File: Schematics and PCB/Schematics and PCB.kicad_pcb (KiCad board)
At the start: 4 copper layers, 181 x 150 mm, 599 parts, among them J11 Conn_01x12, J6 UPSTREAM, J7 DOWNSTREAM_3, J8 DOWNSTREAM_1, J9 DOWNSTREAM_2, Q1 FDN340P, Q2 FDN340P, Q3 FDN340P, Q4 FS8205, SW10 1, SW100 NUMPAD15, SW101 NUMPAD16, SW102 NUMPAD17, SW103 NUMPAD18, SW104 NUMPAD19, SW105 NUMPAD20, SW108 Battery Switch, SW11 2, SW12 3, SW13 4, SW14 5, SW15 6, SW16 TAB, SW17 Q, SW18 W, SW19 E, SW2 ESC, SW20 R, SW21 T, SW22 MAYUS, SW23 A, SW24 S, SW25 D, SW26 F, SW27 G, SW28 L_SHIFT, SW29 Z, SW3 F1, SW30 X, SW31 C, SW32 V, SW33 B, SW34 L_CRTL, SW35 OS, SW36 L_ALT, SW37 L_SPACE, SW38 F7, SW39 F8, SW4 F2, SW40 F9, SW41 F10, SW42 F11, SW43 F12, SW44 PRT_SCR, SW45 DEL, SW46 7, SW47 8, SW48 9, SW49 0, SW5 F3, SW50 -, SW51 =, SW52 BACKSPACE, SW53 MACRO1, SW54 Y, SW55 U, SW56 I, SW57 O, SW58 P, SW59 [, SW6 F4, SW60 ], SW61 \, SW62 H, SW63 J, SW64 K, SW65 L, SW66 ;, SW67 ', SW68 ENTER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

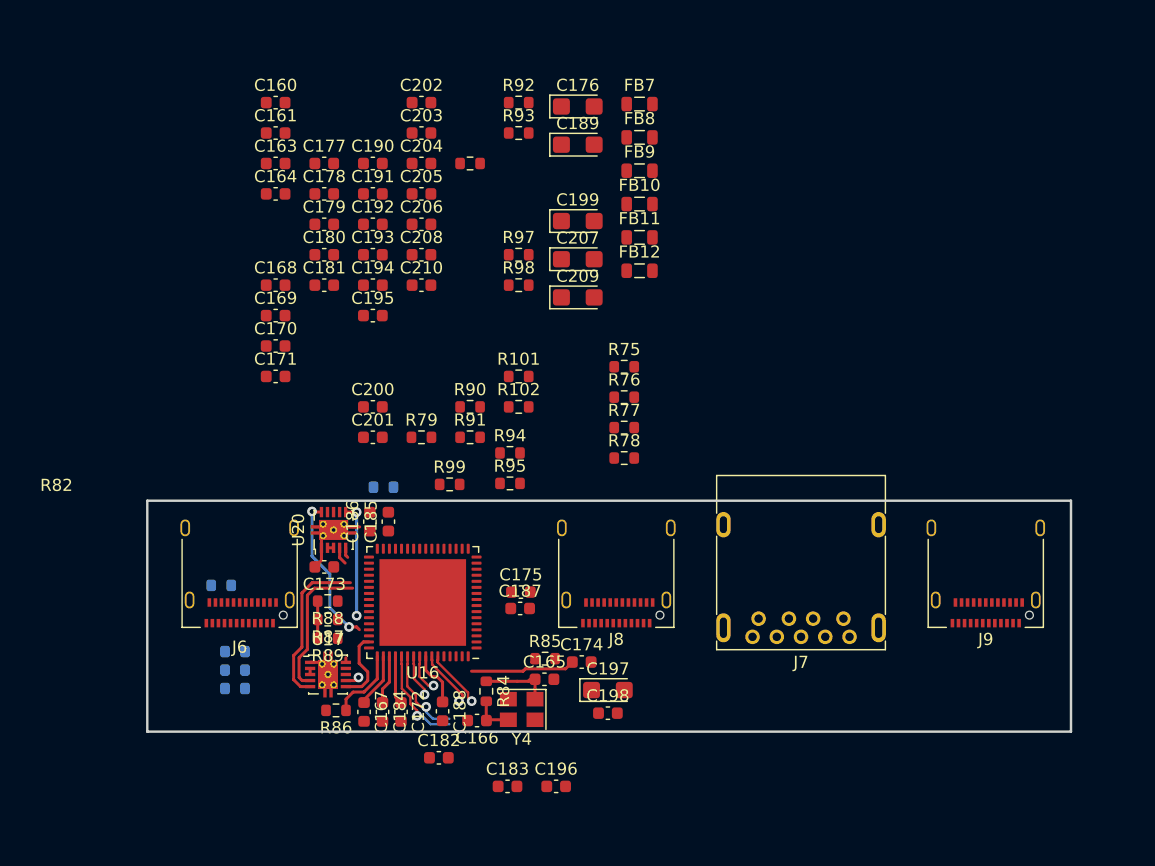
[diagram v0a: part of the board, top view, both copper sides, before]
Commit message: route most of the differential pairs
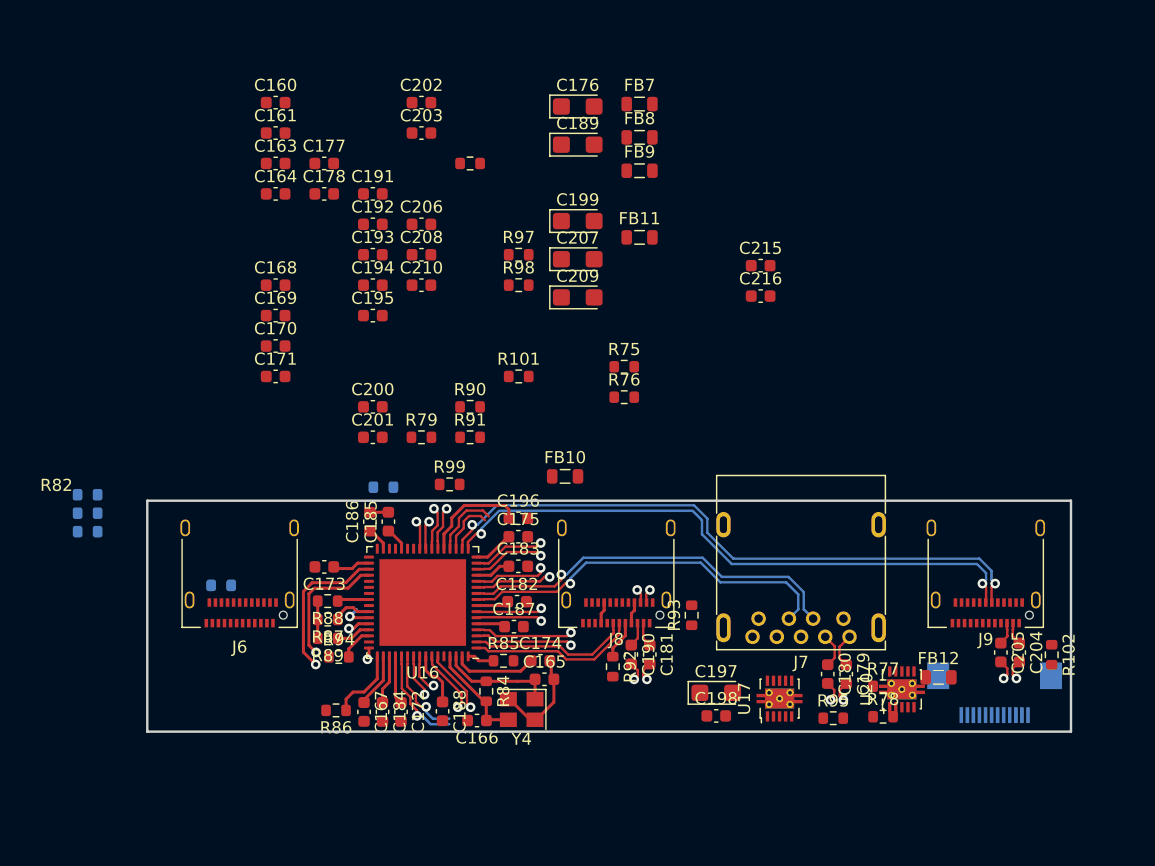
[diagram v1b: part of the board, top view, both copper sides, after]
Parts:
- added C215: 100n, Capacitor_SMD:C_0603_1608Metric, F.Cu at (260.1, 75.9)
- added C216: 100n, Capacitor_SMD:C_0603_1608Metric, F.Cu at (260.1, 78.4)
- added J10: Conn_01x12, Connector_FFC-FPC:Hirose_FH12-12S-0.5SH_1x12-1MP_P0.50mm_Horizontal, B.Cu at (279.4, 111.1)
- moved C204 63.7 mm to (281.5, 107.8), turned to -90 degrees
- moved C205 61.0 mm to (280.0, 107.8), turned to -90 degrees
- moved C179 56.8 mm to (267.2, 109.6), turned to -90 degrees
- moved C180 54.1 mm to (265.7, 109.6), turned to -90 degrees
- moved U20 48.7 mm to (271.8, 110.8)
- moved R102 48.5 mm to (284.2, 108.0), turned to -90 degrees
- moved R92 47.2 mm to (248.0, 108.9), turned to -90 degrees
- moved C190 45.8 mm to (249.5, 107.9), turned to -90 degrees
- moved R93 42.3 mm to (254.5, 104.7), turned to 90 degrees
- moved FB12 41.6 mm to (274.8, 109.8)
- moved C181 40.6 mm to (251.0, 107.9), turned to -90 degrees
- moved U17 37.3 mm to (261.7, 111.6), turned to 90 degrees
- moved R95 33.0 mm to (266.1, 113.2)
- moved R77 30.2 mm to (270.2, 110.6)
- moved R78 30.2 mm to (270.2, 113.1)
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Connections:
- C179 pad 1: /USB Hub/DN3_SSTX_CAP_P -> /USB Hub/DN2_SSTX_CAP_P
- C179 pad 2: /USB Hub/DN3_SSTX_P -> /USB Hub/DN2_SSTX_P
- C180 pad 1: /USB Hub/DN3_SSTX_CAP_N -> /USB Hub/DN2_SSTX_CAP_N
- C180 pad 2: /USB Hub/DN3_SSTX_N -> /USB Hub/DN2_SSTX_N
- C201 pad 1: /USB Hub/DN2_VBUS -> /USB Hub/DN3_VBUS
- C204 pad 1: /USB Hub/DN2_SSTX_CAP_P -> /USB Hub/DN3_SSTX_CAP_P
- C204 pad 2: /USB Hub/DN2_SSTX_P -> /USB Hub/DN3_SSTX_P
- C205 pad 1: /USB Hub/DN2_SSTX_CAP_N -> /USB Hub/DN3_SSTX_CAP_N
- C205 pad 2: /USB Hub/DN2_SSTX_N -> /USB Hub/DN3_SSTX_N
- FB12 pad 2: /USB Hub/DN2_VBUS -> /USB Hub/DN3_VBUS
- J7 pad 2: /USB Hub/DN3_N -> /USB Hub/DN2_N
- J7 pad 3: /USB Hub/DN3_P -> /USB Hub/DN2_P
- J7 pad 5: /USB Hub/DN3_SSRX_N -> /USB Hub/DN2_SSRX_N
- J7 pad 6: /USB Hub/DN3_SSRX_P -> /USB Hub/DN2_SSRX_P
- J7 pad 8: /USB Hub/DN3_SSTX_CAP_N -> /USB Hub/DN2_SSTX_CAP_N
- J7 pad 9: /USB Hub/DN3_SSTX_CAP_P -> /USB Hub/DN2_SSTX_CAP_P
- J9 pad A2: /USB Hub/DN2_SSTX_CAP_P -> /USB Hub/DN3_SSTX_CAP_P
- J9 pad A3: /USB Hub/DN2_SSTX_CAP_N -> /USB Hub/DN3_SSTX_CAP_N
- J9 pad A6: /USB Hub/DN2_P -> /USB Hub/DN3_P
- J9 pad A7: /USB Hub/DN2_N -> /USB Hub/DN3_N
- J9 pad B10: /USB Hub/DN2_SSRX_N -> /USB Hub/DN3_SSRX_N
- J9 pad B11: /USB Hub/DN2_SSRX_P -> /USB Hub/DN3_SSRX_P
- J9 pad B6: /USB Hub/DN2_P -> /USB Hub/DN3_P
- J9 pad B7: /USB Hub/DN2_N -> /USB Hub/DN3_N
- U16 pad 24: /Main IC1/D+ -> /USB Hub/DN4_P
- U16 pad 25: /Main IC1/D- -> /USB Hub/DN4_N
- U16 pad 26: unconnected-(U16-USB_SSTXP_DN4-Pad26) -> /USB Hub/DN4_SSTX_P
- U16 pad 27: unconnected-(U16-USB_SSTXM_DN4-Pad27) -> /USB Hub/DN4_SSTX_N
- U16 pad 29: unconnected-(U16-USB_SSRXP_DN4-Pad29) -> /USB Hub/DN4_SSRX_P
- U16 pad 30: unconnected-(U16-USB_SSRXM_DN4-Pad30) -> /USB Hub/DN4_SSRX_N
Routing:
- net /USB Hub/DN3_SSTX_N: track 0.00 -> 55.6 mm, vias 0 -> 1
- net /USB Hub/DN3_SSTX_P: track 0.00 -> 55.3 mm, vias 0 -> 1
- net /USB Hub/DN3_N: track 0.00 -> 51.6 mm, vias 0 -> 2
- net /USB Hub/DN3_P: track 0.00 -> 50.1 mm, vias 0 -> 2
- net /USB Hub/DN2_SSTX_P: track 0.00 -> 43.4 mm, vias 0 -> 2
- net /USB Hub/DN2_SSTX_N: track 0.00 -> 42.6 mm, vias 0 -> 2
- net /USB Hub/DN2_SSRX_P: track 0.00 -> 33.7 mm, vias 0 -> 1
- net /USB Hub/DN1_SSRX_P: track 0.00 -> 33.5 mm, vias 0 -> 2
- net /USB Hub/DN2_SSRX_N: track 0.00 -> 32.9 mm, vias 0 -> 1
- net /USB Hub/DN1_SSRX_N: track 0.00 -> 32.7 mm, vias 0 -> 2
- net /USB Hub/DN2_N: track 0.00 -> 32.2 mm, vias 0 -> 1
- net /USB Hub/DN2_P: track 0.00 -> 31.5 mm, vias 0 -> 1
- net /USB Hub/1V1_HUB: track 8.63 -> 29.5 mm
- net /USB Hub/DN1_SSTX_P: track 0.00 -> 20.4 mm, vias 0 -> 2
- net /USB Hub/DN1_SSTX_N: track 0.00 -> 19.7 mm, vias 0 -> 2
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
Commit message: Differential pairs routed on the hub
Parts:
- R82: moved to B.Cu
- moved C189 66.9 mm to (200.2, 115.6)
- moved R96 59.3 mm to (261.4, 114.8)
- moved C176 58.7 mm to (214.1, 112.5), turned to 180 degrees
- moved FB10 44.2 mm to (205.7, 115.3)
- moved C163 42.5 mm to (222.3, 109.9), turned to -90 degrees
- moved C164 40.0 mm to (220.8, 109.9), turned to -90 degrees
- moved C215 38.9 mm to (277.1, 110.9), turned to -90 degrees
- moved R82 38.3 mm to (215.7, 99.7), turned to 180 degrees
- moved C216 37.5 mm to (278.9, 110.9), turned to -90 degrees
- moved FB7 18.5 mm to (232.2, 66.6)
- moved R102 13.8 mm to (273.0, 116.1)
- moved R100 11.1 mm to (218.3, 91.2)
- moved C185 5.33 mm to (224.2, 97.6), turned to 180 degrees
- moved C186 4.35 mm to (224.2, 99.2), turned to 180 degrees
- moved FB12 3.03 mm to (272.7, 107.7)
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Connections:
- C172 pad 1: +3V3 -> /USB Hub/3V3_HUB_FILTER
- C173 pad 1: +3V3 -> /USB Hub/3V3_HUB_FILTER
- C174 pad 1: +3V3 -> /USB Hub/3V3_HUB_FILTER
- C175 pad 1: +3V3 -> /USB Hub/3V3_HUB_FILTER
- C176 pad 1: +3V3 -> /USB Hub/3V3_HUB_FILTER
- C182 pad 1: /USB Hub/1V1_HUB -> /USB Hub/1V1_HUB_FILTER
- C183 pad 1: /USB Hub/1V1_HUB -> /USB Hub/1V1_HUB_FILTER
- C184 pad 1: /USB Hub/1V1_HUB -> /USB Hub/1V1_HUB_FILTER
- C185 pad 1: /USB Hub/1V1_HUB -> /USB Hub/1V1_HUB_FILTER
- C186 pad 1: /USB Hub/1V1_HUB -> /USB Hub/1V1_HUB_FILTER
- C187 pad 1: /USB Hub/1V1_HUB -> /USB Hub/1V1_HUB_FILTER
- C188 pad 1: /USB Hub/1V1_HUB -> /USB Hub/1V1_HUB_FILTER
- C189 pad 1: /USB Hub/1V1_HUB -> /USB Hub/1V1_HUB_FILTER
- C203 pad 1: +3V3 -> /USB Hub/3V3_HUB
- FB10 pad 2: /USB Hub/1V1_HUB -> /USB Hub/1V1_HUB_FILTER
- FB7 pad 1: +3V3 -> /USB Hub/3V3_HUB
- FB7 pad 2: +3V3 -> /USB Hub/3V3_HUB_FILTER
- U16 pad 13: /USB Hub/1V1_HUB -> /USB Hub/1V1_HUB_FILTER
- U16 pad 16: +3V3 -> /USB Hub/3V3_HUB_FILTER
- U16 pad 21: /USB Hub/1V1_HUB -> /USB Hub/1V1_HUB_FILTER
- U16 pad 28: /USB Hub/1V1_HUB -> /USB Hub/1V1_HUB_FILTER
- U16 pad 31: /USB Hub/1V1_HUB -> /USB Hub/1V1_HUB_FILTER
- U16 pad 34: +3V3 -> /USB Hub/3V3_HUB_FILTER
- U16 pad 5: /USB Hub/1V1_HUB -> /USB Hub/1V1_HUB_FILTER
- U16 pad 51: /USB Hub/1V1_HUB -> /USB Hub/1V1_HUB_FILTER
- U16 pad 52: +3V3 -> /USB Hub/3V3_HUB_FILTER
- U16 pad 57: /USB Hub/1V1_HUB -> /USB Hub/1V1_HUB_FILTER
- U16 pad 63: +3V3 -> /USB Hub/3V3_HUB_FILTER
- U16 pad 8: /USB Hub/1V1_HUB -> /USB Hub/1V1_HUB_FILTER
- U19 pad 5: +3V3 -> /USB Hub/3V3_HUB
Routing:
- net /USB Hub/DN4_P: track 2.37 -> 81.3 mm
- net /USB Hub/DN4_N: track 2.37 -> 79.9 mm
- net /USB Hub/DN4_SSRX_P: track 0.00 -> 75.6 mm, vias 0 -> 2
- net /USB Hub/DN4_SSRX_N: track 0.00 -> 74.8 mm, vias 0 -> 2
- net /USB Hub/DN4_SSTX_N: track 0.00 -> 72.3 mm, vias 0 -> 2
- net /USB Hub/DN4_SSTX_P: track 0.00 -> 70.8 mm, vias 0 -> 2
- net /USB Hub/UP_P: track 8.38 -> 65.0 mm, vias 1 -> 3
- net /USB Hub/DN3_SSRX_N: track 3.62 -> 59.7 mm, vias 1 -> 2
- net /USB Hub/DN3_SSRX_P: track 3.62 -> 59.6 mm, vias 1 -> 2
- net /USB Hub/UP_N: track 7.64 -> 60.3 mm, vias 1 -> 3
- net /USB Hub/UP_SSRX_N: track 5.34 -> 41.6 mm, vias 1 -> 2
- net /USB Hub/UP_SSRX_P: track 5.34 -> 40.2 mm, vias 1 -> 2
- net /USB Hub/1V1_HUB_FILTER: track 0.00 -> 30.3 mm
- net GND: track 1422.4 -> 1450.3 mm, vias 26 -> 30
- net /USB Hub/UP_VBUS: track 0.00 -> 25.3 mm
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
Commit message: restarted hub layout
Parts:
- added C162: 10u, Capacitor_Tantalum_SMD:CP_EIA-3216-18_Kemet-A, F.Cu at (408.0, 144.2)
- C160, C161, C168, C169, C170, C171, C176, C189, C191, C192, C193, C194, C197, C198, C199, C200, C206, C207, C208, C209, C210, C215, C216, FB10, FB11, FB7, R101, R102, R79, R90, R91, R92, R93, R94, R95, R97, R98, R99, U17, U20: moved to B.Cu
- R80, R81: moved to F.Cu
- moved U18 334.8 mm to (493.4, 140.3)
- moved U19 330.0 mm to (493.4, 133.7), turned to 180 degrees
- moved C191 274.9 mm to (492.6, 145.1), turned to 180 degrees
- moved C195 273.6 mm to (496.3, 134.5), turned to -90 degrees
- moved C203 270.8 mm to (493.4, 136.2)
- moved C202 269.7 mm to (490.6, 139.6), turned to 90 degrees
- moved R100 263.7 mm to (478.4, 134.6), turned to -90 degrees
- moved C194 263.7 mm to (485.9, 133.5), turned to 90 degrees
- moved C192 261.9 mm to (482.8, 133.5), turned to 90 degrees
- moved C177 260.5 mm to (471.6, 148.8), turned to 90 degrees
- moved C201 258.3 mm to (480.4, 145.6)
- moved FB11 256.0 mm to (495.9, 145.1), turned to 180 degrees
- moved C196 255.6 mm to (493.4, 137.8), turned to 180 degrees
- moved C210 254.8 mm to (477.9, 144.9)
- moved R98 253.2 mm to (486.6, 135.8)
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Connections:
- FB11 pad 1: /V_USB -> /USB Hub/DN4_CONN
- J10 pad 1: /USB Hub/DN4_VBUS -> /USB Hub/DN4_CONN
- J10 pad 2: /USB Hub/DN4_VBUS -> /USB Hub/DN4_CONN
- J10 pad 5: unconnected-(J10-Pin_5-Pad5) -> /USB Hub/1V1_EN
- J10 pad 6: /USB Hub/DN4_P -> /USB Hub/3V3_EN
- J10 pad 7: /USB Hub/DN4_N -> /USB Hub/DN4_P
- J10 pad 8: unconnected-(J10-Pin_8-Pad8) -> /USB Hub/DN4_N
- J6 pad S1: (no net) -> Net-(J6-Shield)
- J8 pad S1: (no net) -> Net-(J8-Shield)
- J9 pad S1: (no net) -> Net-(J9-Shield)
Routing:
- net GND: track 1450.3 -> 1640.7 mm, vias 30 -> 36
- net /USB Hub/UP_VBUS: track 25.3 -> 187.2 mm, vias 0 -> 6
- net /USB Hub/DN4_P: track 81.3 -> 7.35 mm
- net /USB Hub/DN4_N: track 79.9 -> 6.23 mm
- net /USB Hub/DN4_SSTX_N: track 72.3 -> 2.20 mm, vias 2 -> 1
- net /USB Hub/DN4_SSRX_N: track 74.8 -> 5.59 mm, vias 2 -> 1
- net /USB Hub/DN4_SSRX_P: track 75.6 -> 6.42 mm, vias 2 -> 1
- net /USB Hub/DN4_SSTX_P: track 70.8 -> 2.20 mm, vias 2 -> 1
- net /USB Hub/DN3_SSTX_P: track 69.6 -> 1.67 mm, vias 2 -> 1
- net /USB Hub/DN3_SSTX_N: track 68.9 -> 1.67 mm, vias 2 -> 1
- net /USB Hub/3V3_HUB: track 0.00 -> 58.6 mm, vias 0 -> 1
- net /USB Hub/DN3_SSRX_N: track 59.7 -> 2.32 mm, vias 2 -> 1
- net /USB Hub/DN3_SSRX_P: track 59.6 -> 2.32 mm, vias 2 -> 1
- net /USB Hub/~{OVCURR2}: track 2.78 -> 58.4 mm, vias 1 -> 3
- net /USB Hub/~{OVCURR1}: track 2.79 -> 54.8 mm, vias 0 -> 3
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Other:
- board size 181 x 150 mm -> 339.6 x 114.3 mm

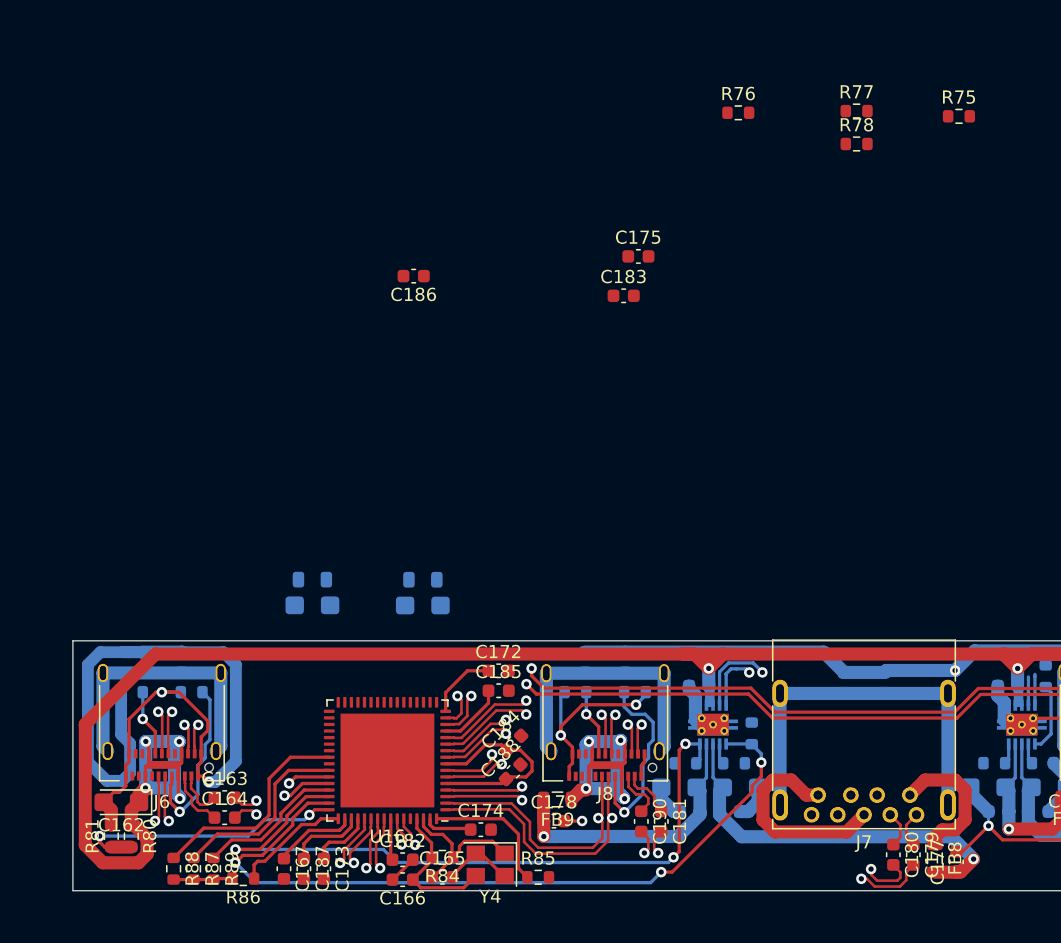
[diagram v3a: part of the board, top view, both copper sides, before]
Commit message: More Hub routing
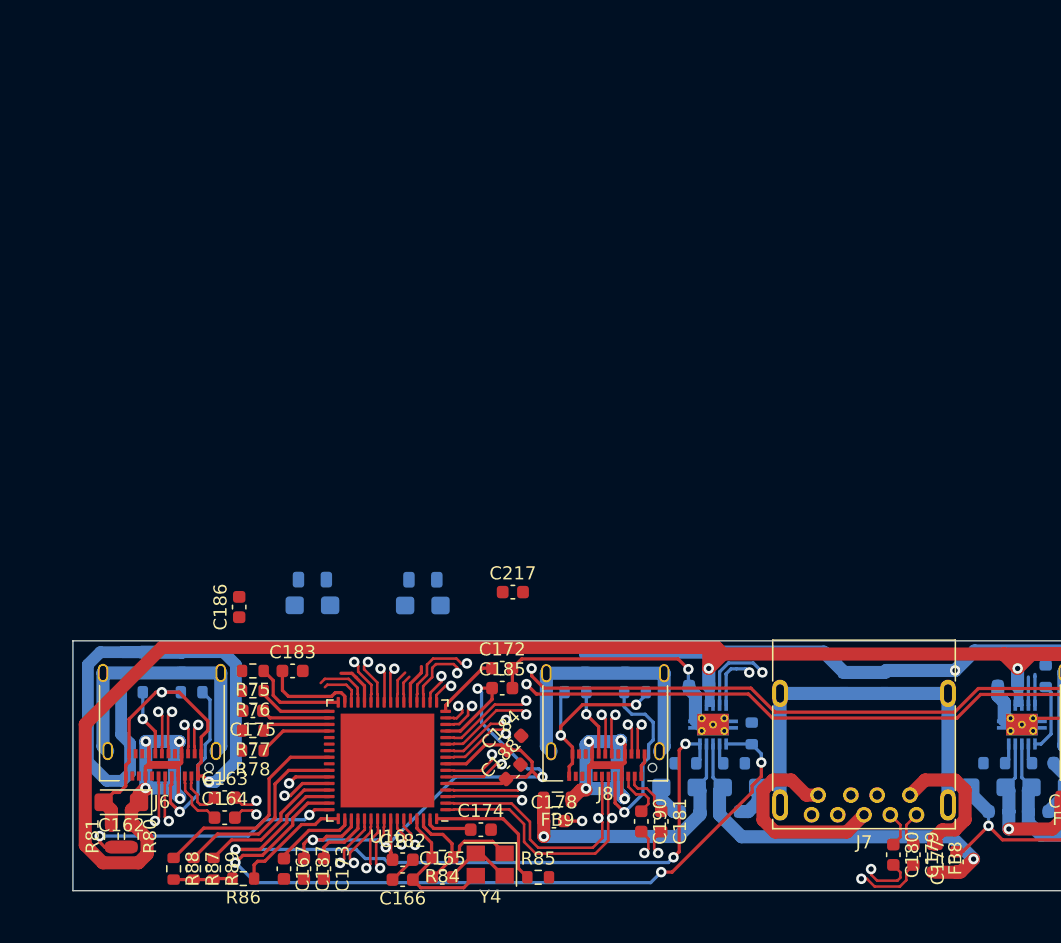
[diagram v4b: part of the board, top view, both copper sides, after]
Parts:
- added C217: 100n, Capacitor_SMD:C_0603_1608Metric, F.Cu at (437.8, 128.2)
- moved R75 68.4 mm to (418.0, 134.2), turned to 180 degrees
- moved R77 65.9 mm to (418.0, 138.8), turned to 180 degrees
- moved R78 65.2 mm to (418.0, 140.3), turned to 180 degrees
- moved R76 57.5 mm to (418.0, 135.7), turned to 180 degrees
- moved C175 45.4 mm to (418.0, 137.2), turned to 180 degrees
- moved C183 38.1 mm to (421.0, 134.2)
- moved C186 28.5 mm to (417.0, 129.3), turned to 90 degrees
- moved C172 0.34 mm to (437.0, 134.0)
- moved C185 0.34 mm to (437.0, 135.5)
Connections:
- C203 pad 1: /USB Hub/3V3_HUB -> +3V3
- FB7 pad 1: /USB Hub/3V3_HUB -> +3V3
- U19 pad 5: /USB Hub/3V3_HUB -> +3V3
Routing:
- net /USB Hub/3V3_HUB: track 58.6 -> 0.00 mm, vias 1 -> 0
- net +3V3: track 0.00 -> 58.6 mm, vias 0 -> 1
- net /USB Hub/1V1_HUB_FILTER: track 29.6 -> 75.8 mm, vias 0 -> 4
- net GND: track 1640.7 -> 1657.5 mm, vias 36 -> 37
- net /USB Hub/BAT_EN_4: track 2.35 -> 9.69 mm
- net /USB Hub/DN3_SSTX_N: track 1.67 -> 8.24 mm, vias 1 -> 2
- net /USB Hub/BAT_EN_3: track 2.20 -> 8.00 mm
- net /USB Hub/BAT_EN_1: track 6.40 -> 12.0 mm
- net /USB Hub/DN3_SSTX_P: track 1.67 -> 7.15 mm, vias 1 -> 2
- net /USB Hub/3V3_HUB_FILTER: track 13.6 -> 19.0 mm
- net /USB Hub/BAT_EN_2: track 4.43 -> 9.63 mm
- net /USB Hub/DN4_SSRX_P: track 6.42 -> 10.8 mm
- net /USB Hub/DN4_SSTX_N: track 2.20 -> 5.83 mm, vias 1 -> 2
- net /USB Hub/DN4_SSTX_P: track 2.20 -> 5.83 mm, vias 1 -> 2
- net /USB Hub/DN4_SSRX_N: track 5.59 -> 8.81 mm
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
